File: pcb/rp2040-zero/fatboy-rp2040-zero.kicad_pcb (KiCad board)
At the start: 2 copper layers, 232.2 x 108.2 mm, 76 parts, among them SW1 SW_Push, U1 Helios

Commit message: remove RST button
Signed-off-by: Anant Thazhemadam <anant.thazhemadam@gmail.com>
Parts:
- removed SW1: SW_Push, marbastlib-various:SW_SKHLLCA010
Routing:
- net RESET: track 85.9 -> 0.00 mm, vias 2 -> 0

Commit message: rerouted rgb
Signed-off-by: Anant Thazhemadam <anant.thazhemadam@gmail.com>
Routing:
- net RGB: track 35.0 -> 33.3 mm, vias 1 -> 0
- net 3V3: track 62.8 -> 62.2 mm, vias 1 -> 0
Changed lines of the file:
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@@
 	)
 	(segment
-		(start 191.590962 148.765861)
-		(end 191.240964 148.415861)
+		(start 188.136209 112.112671)
+		(end 189.38 113.356462)
 		(width 0.25)
-		(layer "F.Cu")
+		(layer "B.Cu")
 		(net 45)
 	)
 	(segment
-		(start 191.991206 115.967672)
-		(end 188.136207 112.112669)
-		(width 0.25)
-		(layer "F.Cu")
-		(net 45)
-	)
-	(segment
-		(start 191.240964 137.915863)
-		(end 191.991209 137.165619)
-		(width 0.25)
-		(layer "F.Cu")
-		(net 45)
-	)
-	(segment
-		(start 191.240964 148.415861)
-		(end 191.240964 137.915863)
-		(width 0.25)
-		(layer "F.Cu")
-		(net 45)
-	)
-	(segment
-		(start 191.991209 137.165619)
-		(end 191.991206 115.967672)
-		(width 0.25)
-		(layer "F.Cu")
-		(net 45)
-	)
-	(via
-		(at 191.590962 148.765861)
-		(size 0.8)
-		(drill 0.4)
-		(layers "F.Cu" "B.Cu")
-		(net 45)
-	)
-	(segment
-		(start 191.617564 151.342464)
-		(end 191.617564 158.867564)
+		(start 189.38 150.2)
+		(end 191.617564 152.437564)
 		(width 0.25)
 		(layer "B.Cu")
@@
 	)
 	(segment
+		(start 191.617564 156.02)
+		(end 191.617564 158.867564)
+		(width 0.25)
+		(layer "B.Cu")
+		(net 45)
+	)
+	(segment
 		(start 191.617564 158.867564)
 		(end 191.617564 168.867571)
@@
 	)
 	(segment
-		(start 191.617564 151.342464)
-		(end 191.590964 151.315861)
+		(start 191.617564 168.867571)
+		(end 193.024997 170.275004)
 		(width 0.25)
 		(layer "B.Cu")
@@
 	)
 	(segment
-		(start 191.590962 148.765861)
-		(end 191.590964 151.315861)
+		(start 191.617564 152.437564)
+		(end 191.617564 156.02)
 		(width 0.25)
 		(layer "B.Cu")
@@
 	)
 	(segment
-		(start 191.617564 168.867571)
-		(end 193.024997 170.275004)
+		(start 189.38 113.356462)
+		(end 189.38 150.2)
 		(width 0.25)
 		(layer "B.Cu")
@@
 	)
 	(segment
-		(start 197.965961 149.490861)
-		(end 197.990963 149.465864)
-		(width 0.25)
-		(layer "F.Cu")
-		(net 47)
-	)
-	(segment
-		(start 190.790963 148.991169)
-		(end 191.290659 149.490863)
-		(width 0.25)
-		(layer "F.Cu")
-		(net 47)
-	)
-	(segment
-		(start 190.790964 132.547427)
-		(end 190.790963 148.991169)
-		(width 0.25)
-		(layer "F.Cu")
-		(net 47)
-	)
-	(segment
-		(start 190.676207 132.432671)
-		(end 190.790964 132.547427)
-		(width 0.25)
-		(layer "F.Cu")
-		(net 47)
-	)
-	(segment
-		(start 191.290659 149.490863)
-		(end 197.965961 149.490861)
-		(width 0.25)
-		(layer "F.Cu")
-		(net 47)
-	)
-	(via
-		(at 197.990963 149.465864)
-		(size 0.8)
-		(drill 0.4)
-		(layers "F.Cu" "B.Cu")
-		(net 47)
-	)
-	(segment
-		(start 198.481208 149.956107)
-		(end 198.48121 160.26879)
+		(start 197.74 158.42)
+		(end 198.475 159.155)
 		(width 0.25)
 		(layer "B.Cu")
@@
 	)
 	(segment
-		(start 197.990963 149.465864)
-		(end 198.481208 149.956107)
+		(start 190.676209 132.432671)
+		(end 190.676209 149.656209)
 		(width 0.25)
 		(layer "B.Cu")
@@
 	)
 	(segment
-		(start 198.48121 160.26879)
+		(start 193.02 152)
+		(end 193.02 157.49)
+		(width 0.25)
+		(layer "B.Cu")
+		(net 47)
+	)
+	(segment
+		(start 198.475 159.155)
 		(end 198.475 160.275)
 		(width 0.25)
 		(layer "B.Cu")
+		(net 47)
+	)
+	(segment
+		(start 193.02 157.49)
+		(end 193.95 158.42)
+		(width 0.25)
+		(layer "B.Cu")
+		(net 47)
+	)
+	(segment
+		(start 190.676209 149.656209)
+		(end 193.02 152)
+		(width 0.25)
+		(layer "B.Cu")
+		(net 47)
+	)
+	(segment
+		(start 193.95 158.42)
+		(end 197.74 158.42)
+		(width 0.25)
+		(layer "B.Cu")

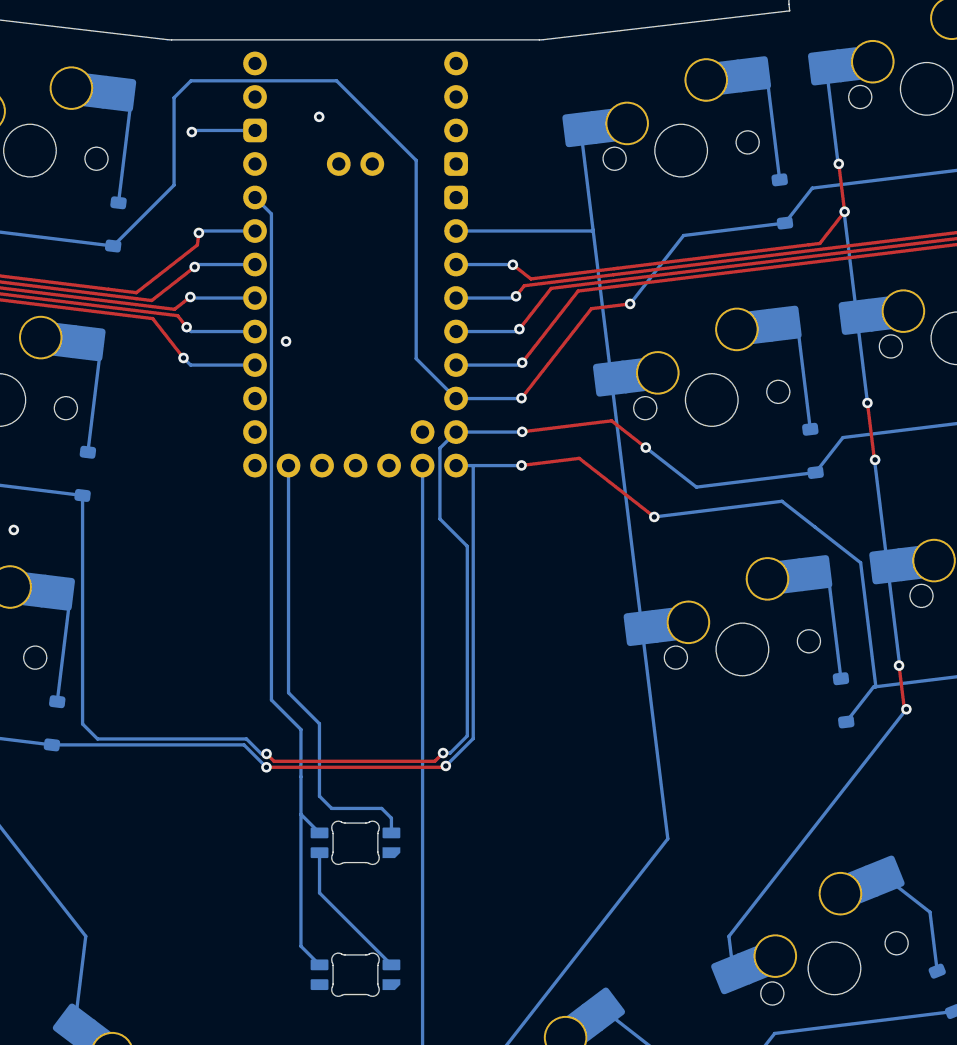
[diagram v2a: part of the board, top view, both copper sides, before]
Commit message: reroute rows
Signed-off-by: Anant Thazhemadam <anant.thazhemadam@gmail.com>
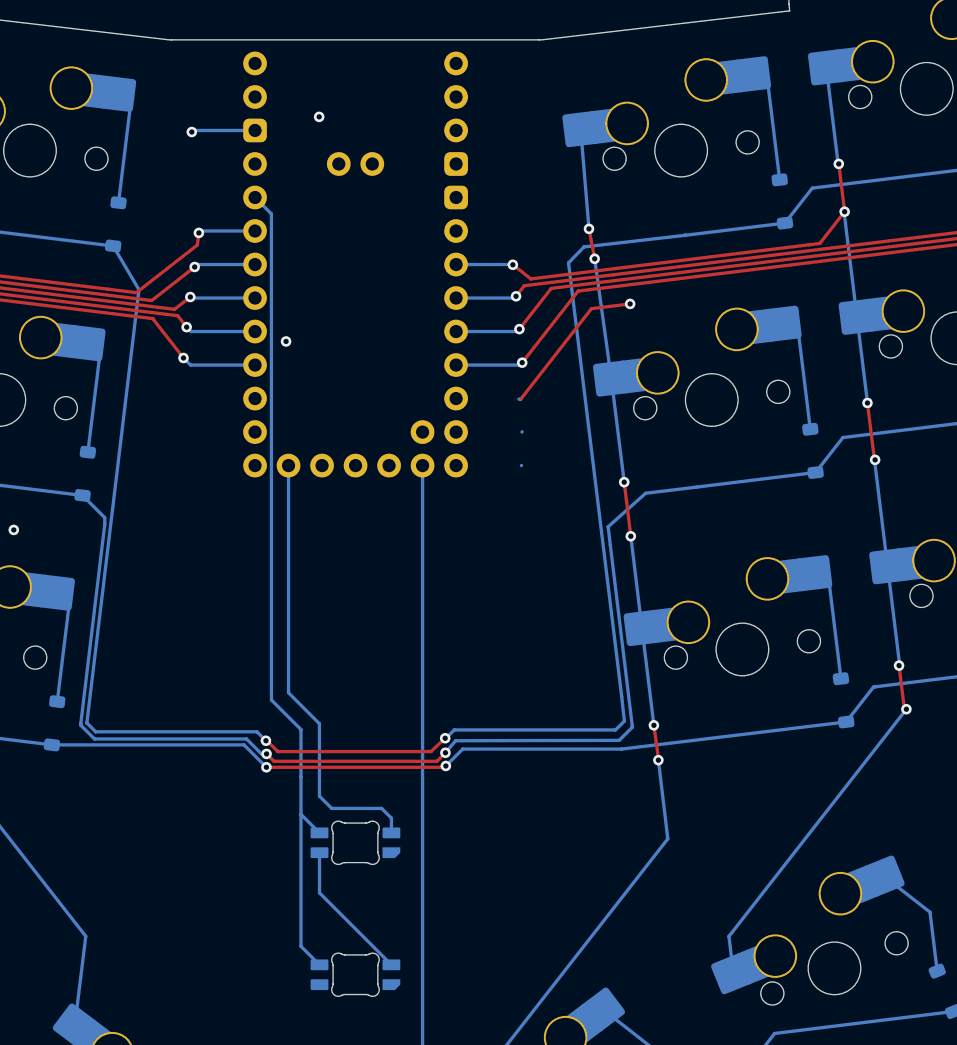
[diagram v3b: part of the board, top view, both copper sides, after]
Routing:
- net ROW1: track 255.1 -> 313.9 mm, vias 2 -> 3
- net ROW3: track 268.0 -> 232.0 mm, vias 4 -> 2
- net COL6: track 92.7 -> 82.4 mm, vias 0 -> 6
- net ROW2: track 272.4 -> 264.8 mm, vias 4 -> 2

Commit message: fix routes
Signed-off-by: Anant Thazhemadam <anant.thazhemadam@gmail.com>
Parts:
- U1: value Helios -> rp2040-zero; footprint PCM_marbastlib-xp-promicroish:Helios_AH_USBup -> mcu:rp2040-zero-tht; moved to F.Cu
- moved U1 3.61 mm to (196.4, 114.9), turned to 0 degrees
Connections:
- U1 pad 10: ROW1 -> ROW4
- U1 pad 11: ROW2 -> ROW3
- U1 pad 12: ROW3 -> ROW2
- U1 pad 13: 5V -> ROW1
- U1 pad 14: GND -> RGB
- U1 pad 15: RESET -> COL1
- U1 pad 16: 3V3 -> COL2
- U1 pad 17: COL5 -> COL3
- U1 pad 19: COL3 -> COL5
- U1 pad 20: COL2 -> unconnected-(U1-29-Pad20)
- U1 pad 21: COL1 -> 3V3
- U1 pad 22: unconnected-(U1-P20-Pad22) -> GND
- U1 pad 23: unconnected-(U1-P23-Pad23) -> 5V
- U1 pad 3: GND -> unconnected-(U1-2-Pad3)
- U1 pad 4: GND -> unconnected-(U1-3-Pad4)
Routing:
- net ROW3: track 232.0 -> 262.5 mm, vias 2 -> 4
- net ROW2: track 264.8 -> 294.2 mm, vias 2 -> 4
- net RGB: track 33.3 -> 60.9 mm
- net 3V3: track 62.2 -> 83.5 mm
- net ROW1: track 313.9 -> 330.5 mm, vias 3 -> 4
- net COL6: track 82.4 -> 91.9 mm
- net ROW4: track 188.0 -> 195.0 mm

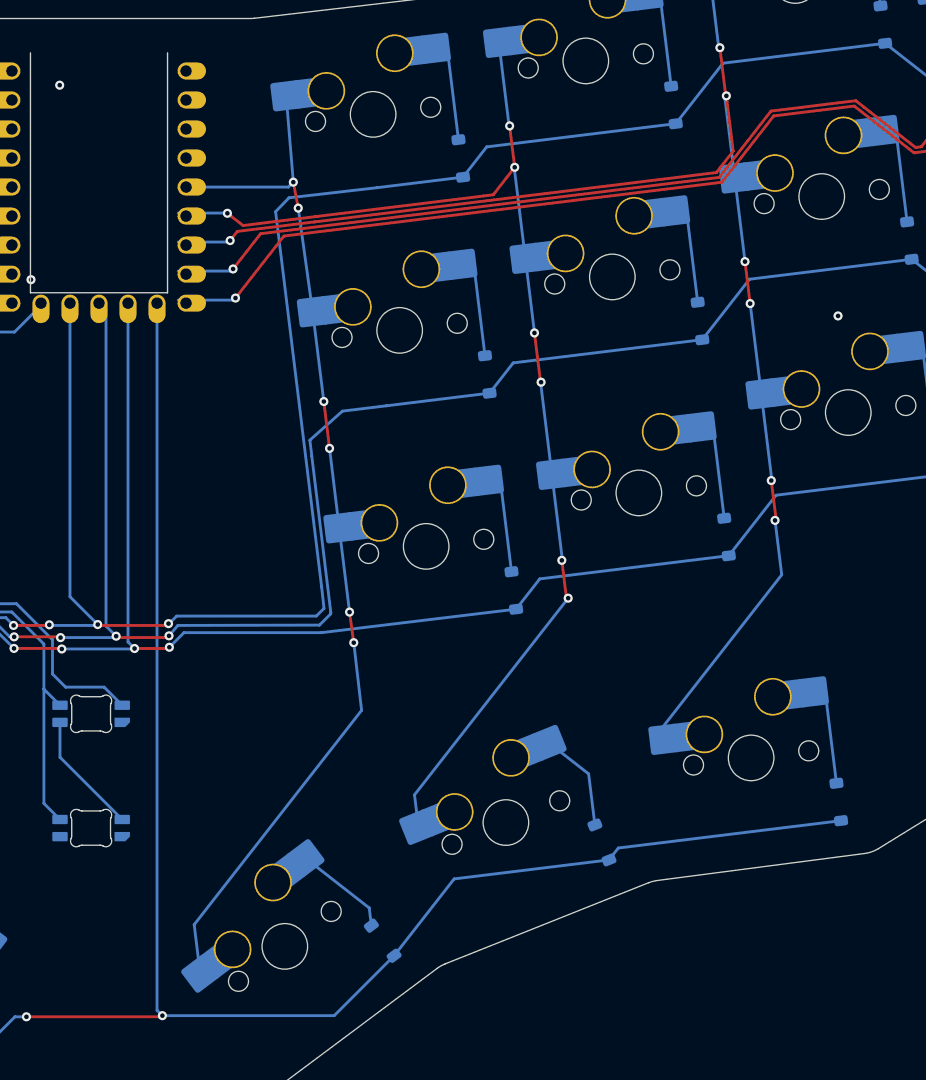
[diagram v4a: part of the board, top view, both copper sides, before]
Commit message: rp2040-zero: finish up design
* Move rows and column labels to digital pins instead of analog, since
the latter has been reported to apparently have random issues with
registering keypresses sometimes
* Re-route tracks
* Remove unnecessary labels
* Remove shift register, since this will require a significant re-write
and re-routing for everything
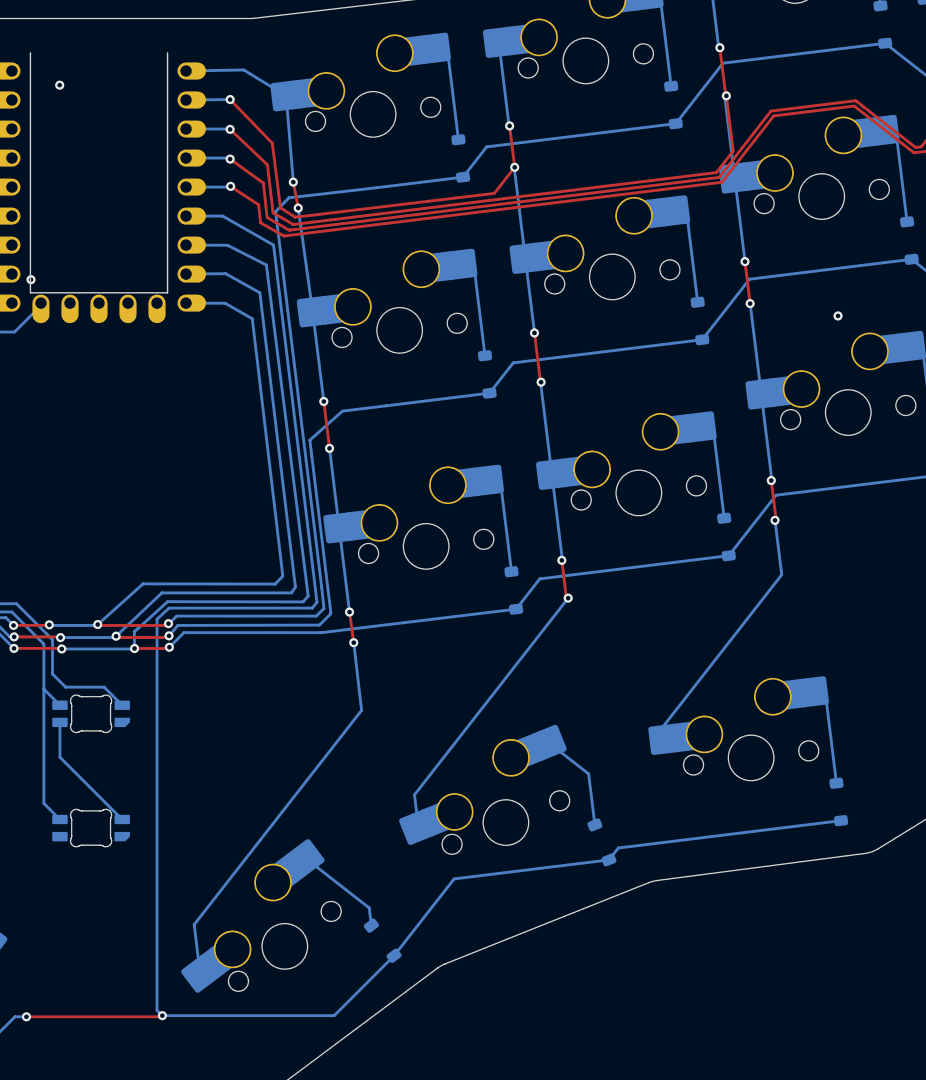
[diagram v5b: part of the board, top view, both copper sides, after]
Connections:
- net 3V3 renamed +3V3
- net 5V renamed +5V
- U1 pad 1: unconnected-(U1-0-Pad1) -> COL6
- U1 pad 10: ROW4 -> unconnected-(U1-9-Pad10)
- U1 pad 11: ROW3 -> unconnected-(U1-10-Pad11)
- U1 pad 12: ROW2 -> unconnected-(U1-11-Pad12)
- U1 pad 13: ROW1 -> unconnected-(U1-12-Pad13)
- U1 pad 2: unconnected-(U1-1-Pad2) -> COL7
- U1 pad 3: unconnected-(U1-2-Pad3) -> COL8
- U1 pad 4: unconnected-(U1-3-Pad4) -> COL9
- U1 pad 5: COL6 -> COL10
- U1 pad 6: COL7 -> ROW4
- U1 pad 7: COL8 -> ROW3
- U1 pad 8: COL9 -> ROW2
- U1 pad 9: COL10 -> ROW1
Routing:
- net ROW4: track 195.0 -> 221.8 mm
- net ROW3: track 262.5 -> 286.6 mm
- net ROW2: track 294.2 -> 314.8 mm
- net ROW1: track 330.5 -> 348.0 mm
- net COL7: track 105.1 -> 110.8 mm
- net COL8: track 127.3 -> 131.4 mm
- net COL9: track 113.3 -> 114.7 mm
- net COL10: track 133.2 -> 132.0 mm
